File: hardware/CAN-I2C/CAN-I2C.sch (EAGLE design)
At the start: 31 parts, among them Q1 12MHZ, U1 MCP2515(MCP2510)ML, U2 MCP2551, U4 ATTINY816M

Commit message: Silkscreen and routing cleanup
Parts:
- renumbered CAN-RIBBON to RIBBON, U$1 to CAN-IN, U$2 to CAN-OUT
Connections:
- net !OUT_CS!: now also JP1.5; no longer JP1.11
- net +12V: now also JP1.12; no longer JP1.8
- net +3V3: now also JP1.6; no longer JP1.2
- net +5V: now also JP1.2; no longer JP1.6
- net GND: now also JP1.8; no longer JP1.12
- net MISO: now also JP1.11; no longer JP1.9
- net MOSI: now also JP1.9; no longer JP1.7
- net SCK: now also JP1.7; no longer JP1.5
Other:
- moved on the sheet: AD0, DIR

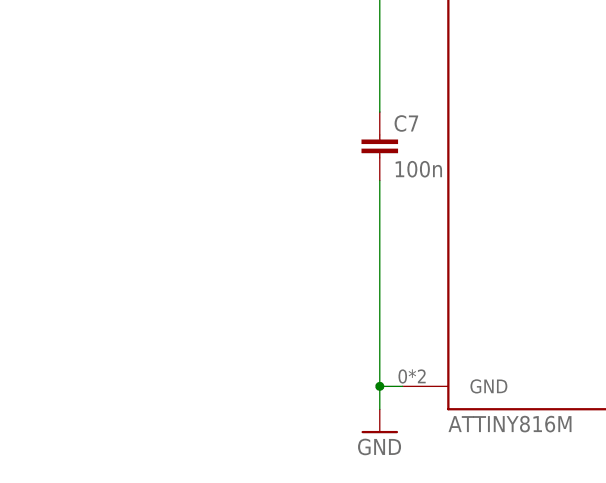
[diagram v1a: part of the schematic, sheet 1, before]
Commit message: Added mounting tabs
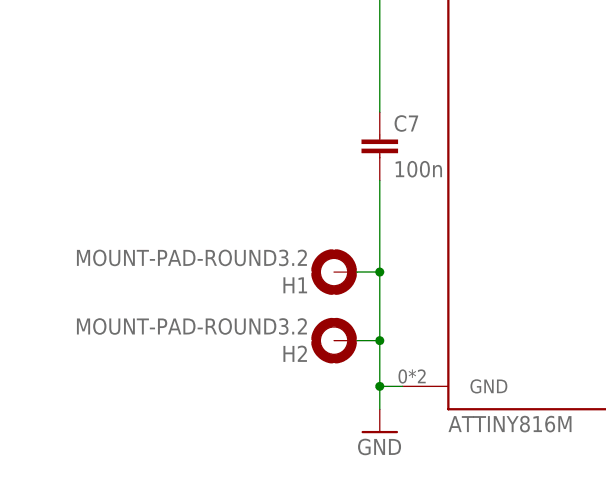
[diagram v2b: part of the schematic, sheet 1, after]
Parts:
- added H1, H2: MOUNT-PAD-ROUND3.2, holes:MOUNT-PAD-ROUND3.2
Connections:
- net GND: now also H1.MOUNT, H2.MOUNT
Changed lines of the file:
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@@
 <part name="GND6" library="supply1" library_urn="urn:adsk.eagle:library:371" deviceset="GND" device=""/>
 <part name="JP4" library="pinhead" library_urn="urn:adsk.eagle:library:325" deviceset="PINHD-2X16" device="" package3d_urn="urn:adsk.eagle:package:22431/2"/>
+<part name="H1" library="holes" library_urn="urn:adsk.eagle:library:237" deviceset="MOUNT-PAD-ROUND" device="3.2" package3d_urn="urn:adsk.eagle:package:14282/1"/>
+<part name="H2" library="holes" library_urn="urn:adsk.eagle:library:237" deviceset="MOUNT-PAD-ROUND" device="3.2" package3d_urn="urn:adsk.eagle:package:14282/1"/>
 </parts>
 <sheets>
@@
 <instance part="P+2" gate="1" x="147.32" y="208.28"/>
 <instance part="P+3" gate="1" x="154.94" y="208.28"/>
+<instance part="H1" gate="G$1" x="33.02" y="40.64" rot="R180"/>
+<instance part="H2" gate="G$1" x="33.02" y="33.02" rot="R180"/>
 </instances>
 <busses>
@@
 <wire x1="38.1" y1="27.94" x2="40.64" y2="27.94" width="0.1524" layer="91"/>
 <pinref part="C7" gate="G$1" pin="2"/>
-<wire x1="38.1" y1="27.94" x2="38.1" y2="50.8" width="0.1524" layer="91"/>
+<wire x1="38.1" y1="27.94" x2="38.1" y2="33.02" width="0.1524" layer="91"/>
 <junction x="38.1" y="27.94"/>
-</segment>
-</net>
+<pinref part="H1" gate="G$1" pin="MOUNT"/>
+<wire x1="38.1" y1="33.02" x2="38.1" y2="40.64" width="0.1524" layer="91"/>
+<wire x1="38.1" y1="40.64" x2="38.1" y2="50.8" width="0.1524" layer="91"/>
+<wire x1="35.56" y1="40.64" x2="38.1" y2="40.64" width="0.1524" layer="91"/>
+<junction x="38.1" y="40.64"/>
+<pinref part="H2" gate="G$1" pin="MOUNT"/>
+<wire x1="35.56" y1="33.02" x2="38.1" y2="33.02" width="0.1524" layer="91"/>
+<junction x="38.1" y="33.02"/>
+</segment>
+</net>
